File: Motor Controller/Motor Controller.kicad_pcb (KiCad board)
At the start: 2 copper layers, 50 x 55.1 mm, 5 parts, among them J1 Conn_01x03_Pin, U1 SN74LV1T34DBV

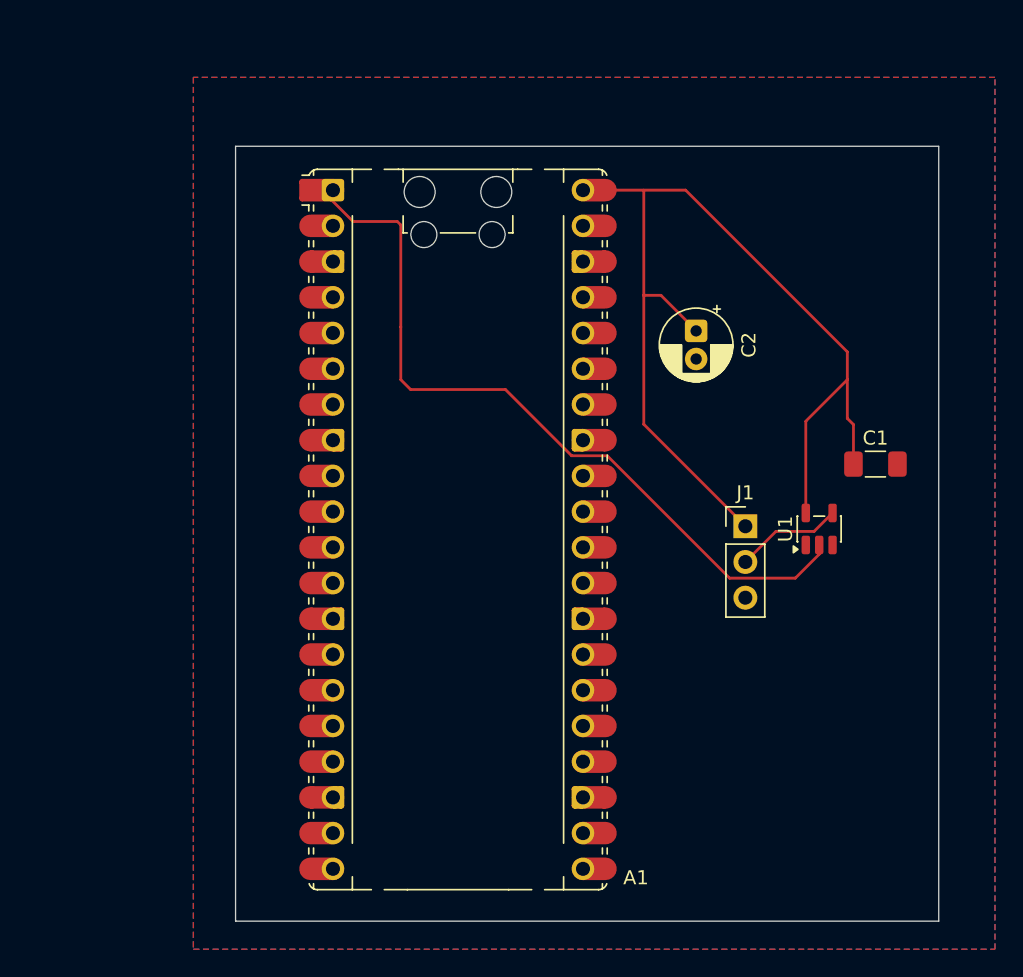
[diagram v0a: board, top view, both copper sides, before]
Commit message: Replaced with revision 2 and made some small fixes; ready for export
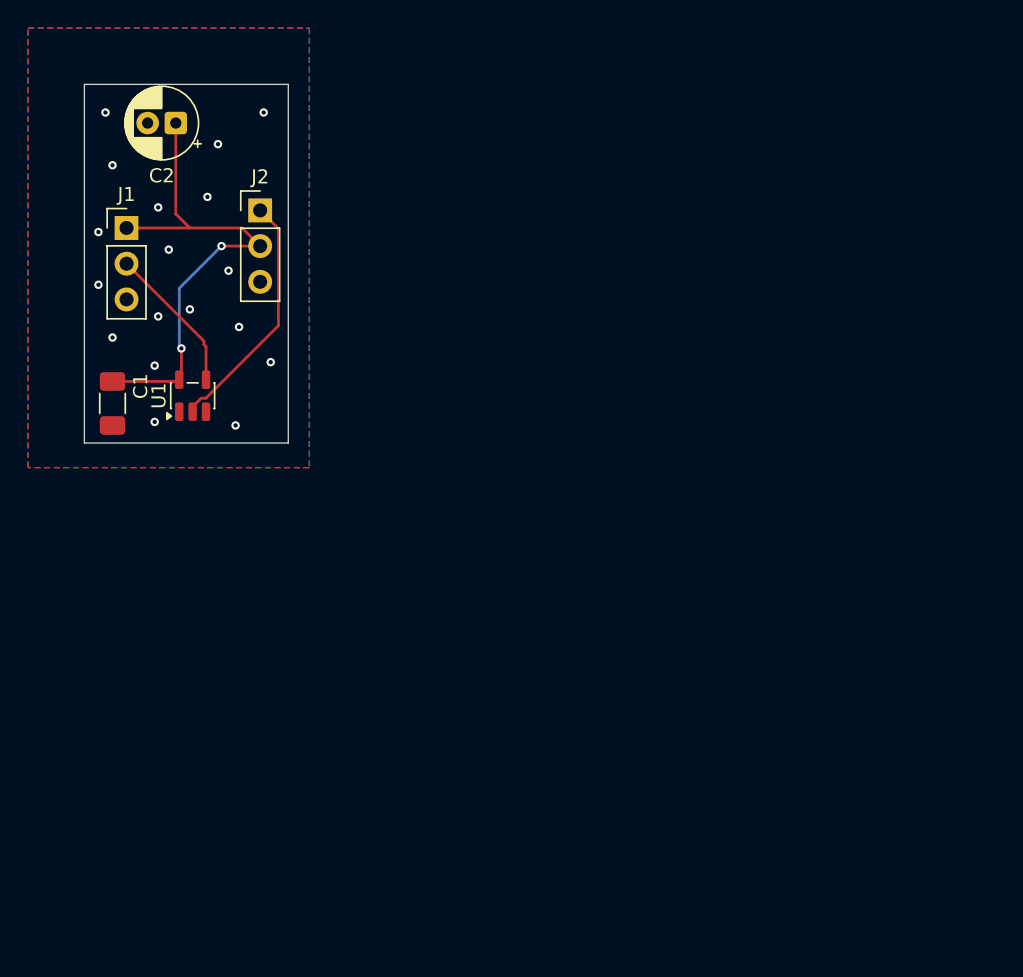
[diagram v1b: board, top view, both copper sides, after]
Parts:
- removed A1: RaspberryPi_Pico, Module:RaspberryPi_Pico_Common_Unspecified
- added J2: Conn_01x03_Pin, Connector_PinHeader_2.54mm:PinHeader_1x03_P2.54mm_Vertical, F.Cu at (132.8, 73.5)
- C1: value 100 Micro-Ferrets -> 100n
- C2: value 100 Micro-Ferrets -> 10u
- moved C1 54.4 mm to (122.2, 87.2), turned to -90 degrees
- moved J1 48.8 mm to (123.2, 74.7)
- moved U1 45.5 mm to (128.0, 86.6)
- moved C2 39.8 mm to (126.8, 67.2), turned to 180 degrees
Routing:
- net VBUS: track 73.8 -> 36.5 mm, vias 0 -> 2
- net Net-(J2-Pin_1): track 54.6 -> 17.6 mm
- net Net-(J1-Pin_2): track 7.64 -> 10.6 mm
- net GND: vias 0 -> 18
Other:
- board size 50 x 55.1 mm -> 14.5 x 25.5 mm
- board text added: "Reid Rev:2 Motor Controller"
